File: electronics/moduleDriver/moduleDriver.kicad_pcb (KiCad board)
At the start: 2 copper layers, 100 x 100 mm, 65 parts, among them J1 Power In, J10 12V SENSE, J2 UART, J3 SENSOR, J4 5V, J5 GND, J8 RS485, J9 RS485, U1 Mega2560Shield, U10 ULN2003A_E, U11 INA219 Breakout Wide (blue), U12 ULN2003A_D, U13 ULN2003A_C, U14 ULN2003A_B, U15 ULN2003A_A, U17 RS485Module, U2 SSD1306_I2C, U3 ULN2003A_L, U31 INA219 Breakout Narrow (purpl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, U32 SP485, U33 INA219BxD, U4 ULN2003A_K, U5 ULN2003A_J, U6 ULN2003A_I, U7 ULN2003A_H, U8 ULN2003A_G, U9 ULN2003A_F

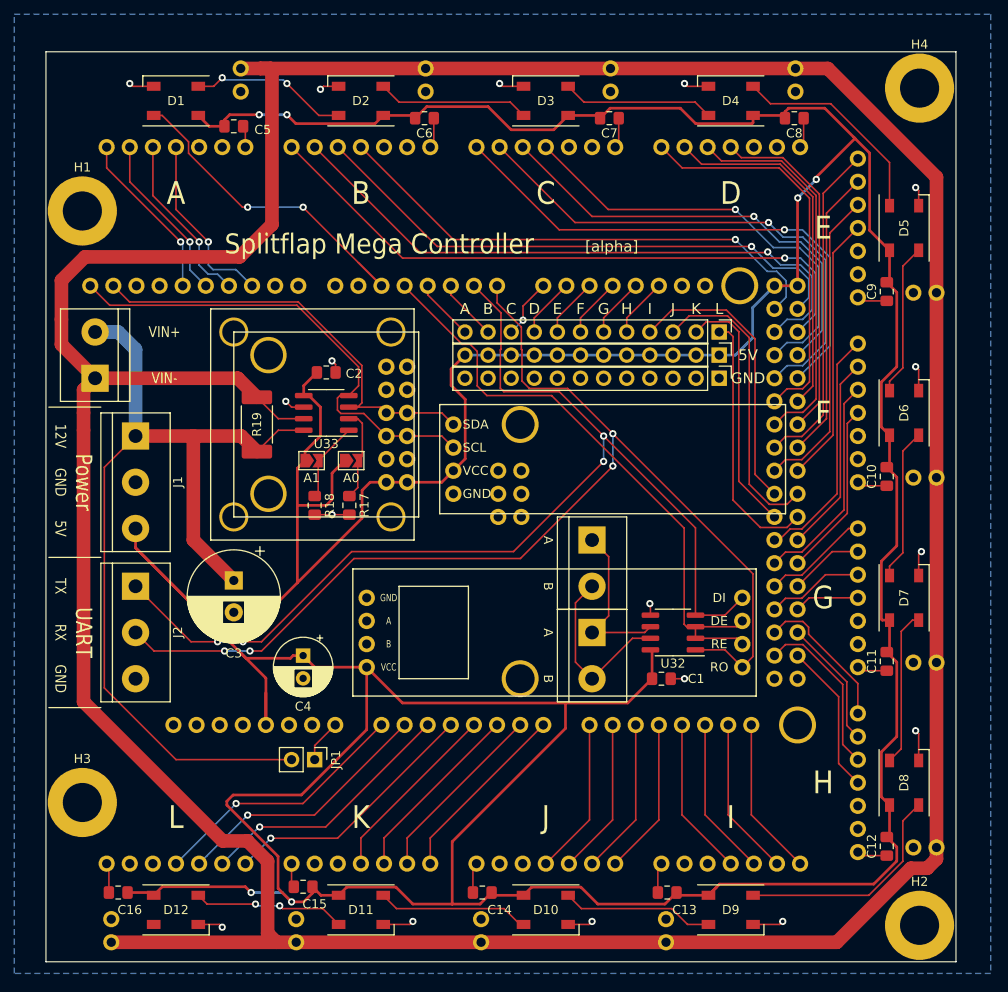
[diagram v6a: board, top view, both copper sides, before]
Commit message: More Mega tweaks for order - moving ULN2003 modules closer to edge
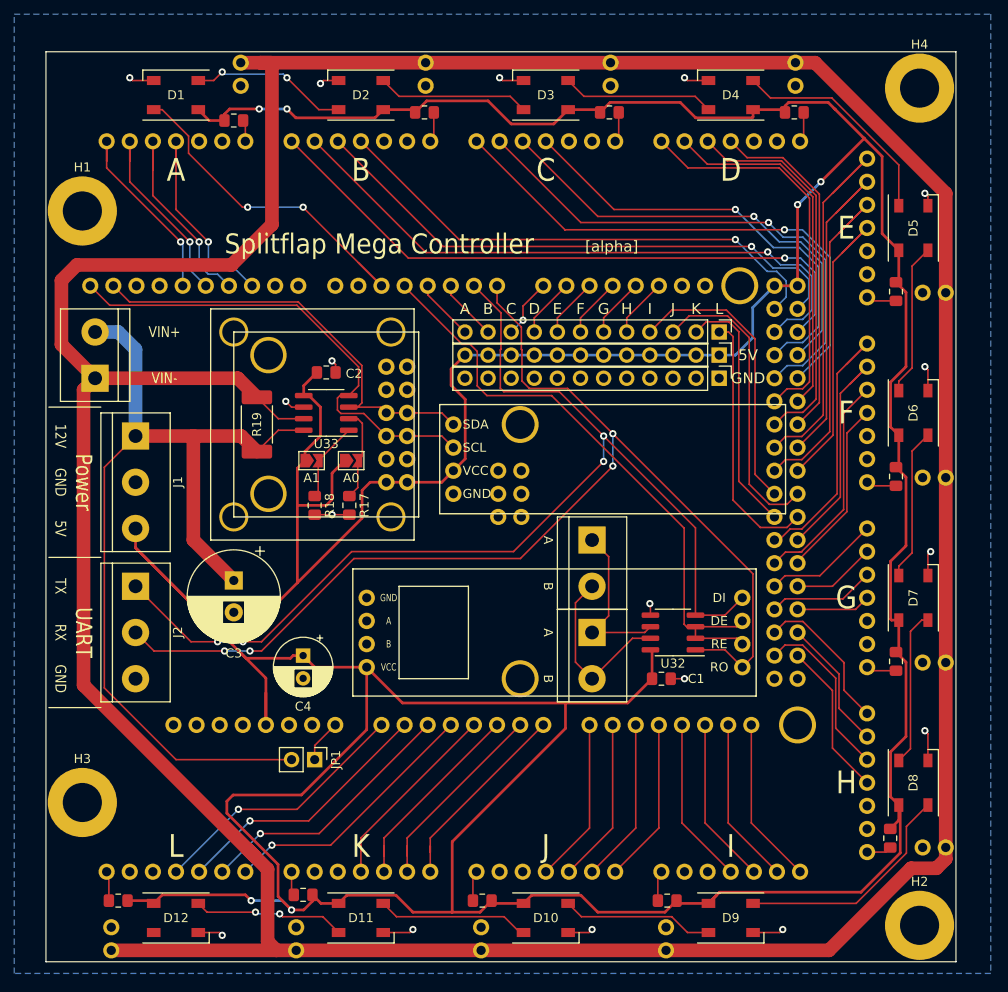
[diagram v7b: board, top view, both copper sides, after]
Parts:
- moved C10 1.02 mm to (113.4, 66.7)
- moved C11 1.02 mm to (113.4, 87.0)
- moved C9 1.02 mm to (113.4, 46.4)
- moved D5 1.02 mm to (115.3, 39.4)
- moved D6 1.02 mm to (115.3, 59.7)
- moved D7 1.02 mm to (115.3, 80.0)
- moved D8 1.02 mm to (115.3, 100.3)
- moved U10 1.02 mm to (110.2, 31.8)
- moved U7 1.02 mm to (110.2, 92.7)
- moved U8 1.02 mm to (110.2, 72.4)
- moved U9 1.02 mm to (110.2, 52.1)
- moved C12 0.97 mm to (112.8, 106.4)
- moved C13 0.89 mm to (88.3, 113.3)
- moved C14 0.89 mm to (67.9, 113.3)
- moved C16 0.89 mm to (27.9, 113.3)
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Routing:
- net +5V: track 568.1 -> 574.5 mm
- net /MOTOR_E_PHASE_A: track 36.6 -> 42.4 mm
- net /MOTOR_E_PHASE_B: track 32.0 -> 37.3 mm
- net /MOTOR_E_PHASE_C: track 34.1 -> 38.9 mm
- net /MOTOR_E_PHASE_D: track 29.4 -> 33.7 mm
- net /MOTOR_F_PHASE_A: track 26.4 -> 30.1 mm
- net /MOTOR_A_PHASE_C: track 19.3 -> 22.5 mm
- net /MOTOR_F_PHASE_B: track 21.8 -> 24.9 mm
- net /MOTOR_A_PHASE_D: track 20.2 -> 22.6 mm
- net /MOTOR_A_PHASE_B: track 18.7 -> 20.9 mm
- net /MOTOR_A_PHASE_A: track 18.7 -> 20.9 mm
- net +12V_Monitored: track 404.7 -> 406.8 mm
- net /MOTOR_K_PHASE_C: track 20.7 -> 22.7 mm
- net /MOTOR_K_PHASE_B: track 21.1 -> 23.1 mm
- net /MOTOR_K_PHASE_A: track 20.4 -> 21.9 mm
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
